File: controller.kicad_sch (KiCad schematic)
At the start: 50 parts, among them U1 TMC4671, U2 74LVC3G17, U3 74LVC3G17

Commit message: Small improvements.
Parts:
- added TP1: EN TestPoint, TestPoint:TestPoint_Pad_D1.0mm, symbol Connector:TestPoint
- C11, C12, C13, C14, C15, C16, C18, C19, C20, C21, C22, C35, C36, C40, C7, C8: MPN CL05B104KB54PNC -> GRM155R71H104KE14J
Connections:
- net DRV_EN: now also TP1.1
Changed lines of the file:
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@@
   (junction (at 149.86 162.56) (diameter 0) (color 0 0 0 0)
   )
+  (junction (at 180.34 26.67) (diameter 0) (color 0 0 0 0)
+  )
   (junction (at 54.61 104.14) (diameter 0) (color 0 0 0 0)
   )
@@
     (stroke (width 0) (type default))
   )
+  (wire (pts (xy 180.34 24.13) (xy 180.34 26.67))
+    (stroke (width 0) (type default))
+  )
   (wire (pts (xy 259.08 109.22) (xy 271.78 109.22))
     (stroke (width 0) (type default))
@@
     (stroke (width 0) (type default))
   )
+  (wire (pts (xy 180.34 26.67) (xy 177.8 26.67))
+    (stroke (width 0) (type default))
+  )
   (wire (pts (xy 234.95 128.27) (xy 232.41 128.27))
     (stroke (width 0) (type default))
@@
     (stroke (width 0) (type default))
   )
-  (wire (pts (xy 182.88 26.67) (xy 177.8 26.67))
+  (wire (pts (xy 182.88 26.67) (xy 180.34 26.67))
     (stroke (width 0) (type default))
   )
@@
       (effects (font (size 1.27 1.27)) hide)
     )
-    (property "MPN" "CL05B104KB54PNC" (at 107.95 167.64 0)
+    (property "MPN" "GRM155R71H104KE14J" (at 107.95 167.64 0)
       (effects (font (size 1.27 1.27)) hide)
     )
@@
       (effects (font (size 1.27 1.27)) hide)
     )
-    (property "MPN" "CL05B104KB54PNC" (at 54.61 128.27 0)
+    (property "MPN" "GRM155R71H104KE14J" (at 54.61 128.27 0)
       (effects (font (size 1.27 1.27)) hide)
     )
@@
       (effects (font (size 1.27 1.27)) hide)
     )
-    (property "MPN" "CL05B104KB54PNC" (at 218.44 162.56 0)
+    (property "MPN" "GRM155R71H104KE14J" (at 218.44 162.56 0)
       (effects (font (size 1.27 1.27)) hide)
     )
@@
       (effects (font (size 1.27 1.27)) hide)
     )
-    (property "MPN" "CL05B104KB54PNC" (at 93.98 167.64 0)
+    (property "MPN" "GRM155R71H104KE14J" (at 93.98 167.64 0)
       (effects (font (size 1.27 1.27)) hide)
     )
@@
       (effects (font (size 1.27 1.27)) hide)
     )
-    (property "MPN" "CL05B104KB54PNC" (at 135.89 167.64 0)
+    (property "MPN" "GRM155R71H104KE14J" (at 135.89 167.64 0)
       (effects (font (size 1.27 1.27)) hide)
     )
@@
       (effects (font (size 1.27 1.27)) hide)
     )
-    (property "MPN" "CL05B104KB54PNC" (at 33.02 157.48 0)
+    (property "MPN" "GRM155R71H104KE14J" (at 33.02 157.48 0)
       (effects (font (size 1.27 1.27)) hide)
     )
@@
       (effects (font (size 1.27 1.27)) hide)
     )
-    (property "MPN" "CL05B104KB54PNC" (at 73.66 86.36 0)
+    (property "MPN" "GRM155R71H104KE14J" (at 73.66 86.36 0)
       (effects (font (size 1.27 1.27)) hide)
     )
@@
       (effects (font (size 1.27 1.27)) hide)
     )
-    (property "MPN" "CL05B104KB54PNC" (at 121.92 167.64 0)
+    (property "MPN" "GRM155R71H104KE14J" (at 121.92 167.64 0)
       (effects (font (size 1.27 1.27)) hide)
     )
@@
       (effects (font (size 1.27 1.27)) hide)
     )
-    (property "MPN" "CL05B104KB54PNC" (at 39.37 128.27 0)
+    (property "MPN" "GRM155R71H104KE14J" (at 39.37 128.27 0)
       (effects (font (size 1.27 1.27)) hide)
     )
@@
       (effects (font (size 1.27 1.27)) hide)
     )
-    (property "MPN" "CL05B104KB54PNC" (at 69.85 109.22 0)
+    (property "MPN" "GRM155R71H104KE14J" (at 69.85 109.22 0)
       (effects (font (size 1.27 1.27)) hide)
     )
@@
       (effects (font (size 1.27 1.27)) hide)
     )
-    (property "MPN" "CL05B104KB54PNC" (at 149.86 167.64 0)
+    (property "MPN" "GRM155R71H104KE14J" (at 149.86 167.64 0)
       (effects (font (size 1.27 1.27)) hide)
     )
@@
       (effects (font (size 1.27 1.27)) hide)
     )
-    (property "MPN" "CL05B104KB54PNC" (at 217.17 38.1 0)
+    (property "MPN" "GRM155R71H104KE14J" (at 217.17 38.1 0)
       (effects (font (size 1.27 1.27)) hide)
     )
@@
     )
   )
+  (symbol (lib_id "Connector:TestPoint") (at 180.34 24.13 0) (unit 1)
+    (in_bom yes) (on_board yes) (dnp no) (fields_autoplaced)
+    (property "Reference" "TP1" (at 182.88 20.193 0)
+      (effects (font (size 1.27 1.27)) (justify left))
+    )
+    (property "Value" "EN TestPoint" (at 182.88 22.733 0)
+      (effects (font (size 1.27 1.27)) (justify left))
+    )
+    (property "Footprint" "TestPoint:TestPoint_Pad_D1.0mm" (at 185.42 24.13 0)
+      (effects (font (size 1.27 1.27)) hide)
+    )
+    (property "Datasheet" "~" (at 185.42 24.13 0)
+      (effects (font (size 1.27 1.27)) hide)
+    )
+    (pin "1")
+    (instances
+      (project "motor-driver"
+        (path "/314549f2-cc46-4559-991a-ae9411f3d209/25794513-4b05-4cf2-b97c-a9dcfa280e83"
+          (reference "TP1") (unit 1)
+        )
+      )
+    )
+  )
   (symbol (lib_id "74xGxx:74LVC3G17") (at 219.71 152.4 270) (unit 4)
     (in_bom yes) (on_board yes) (dnp no)
@@
       (effects (font (size 1.27 1.27)) hide)
     )
-    (property "MPN" "CL05B104KB54PNC" (at 31.75 40.64 0)
+    (property "MPN" "GRM155R71H104KE14J" (at 31.75 40.64 0)
       (effects (font (size 1.27 1.27)) hide)
     )
@@
       (effects (font (size 1.27 1.27)) hide)
     )
-    (property "MPN" "CL05B104KB54PNC" (at 69.85 128.27 0)
+    (property "MPN" "GRM155R71H104KE14J" (at 69.85 128.27 0)
       (effects (font (size 1.27 1.27)) hide)
     )
@@
       (effects (font (size 1.27 1.27)) hide)
     )
-    (property "MPN" "CL05B104KB54PNC" (at 33.02 186.69 0)
+    (property "MPN" "GRM155R71H104KE14J" (at 33.02 186.69 0)
       (effects (font (size 1.27 1.27)) hide)
     )
@@
       (effects (font (size 1.27 1.27)) hide)
     )
-    (property "MPN" "CL05B104KB54PNC" (at 163.83 167.64 0)
+    (property "MPN" "GRM155R71H104KE14J" (at 163.83 167.64 0)
       (effects (font (size 1.27 1.27)) hide)
     )

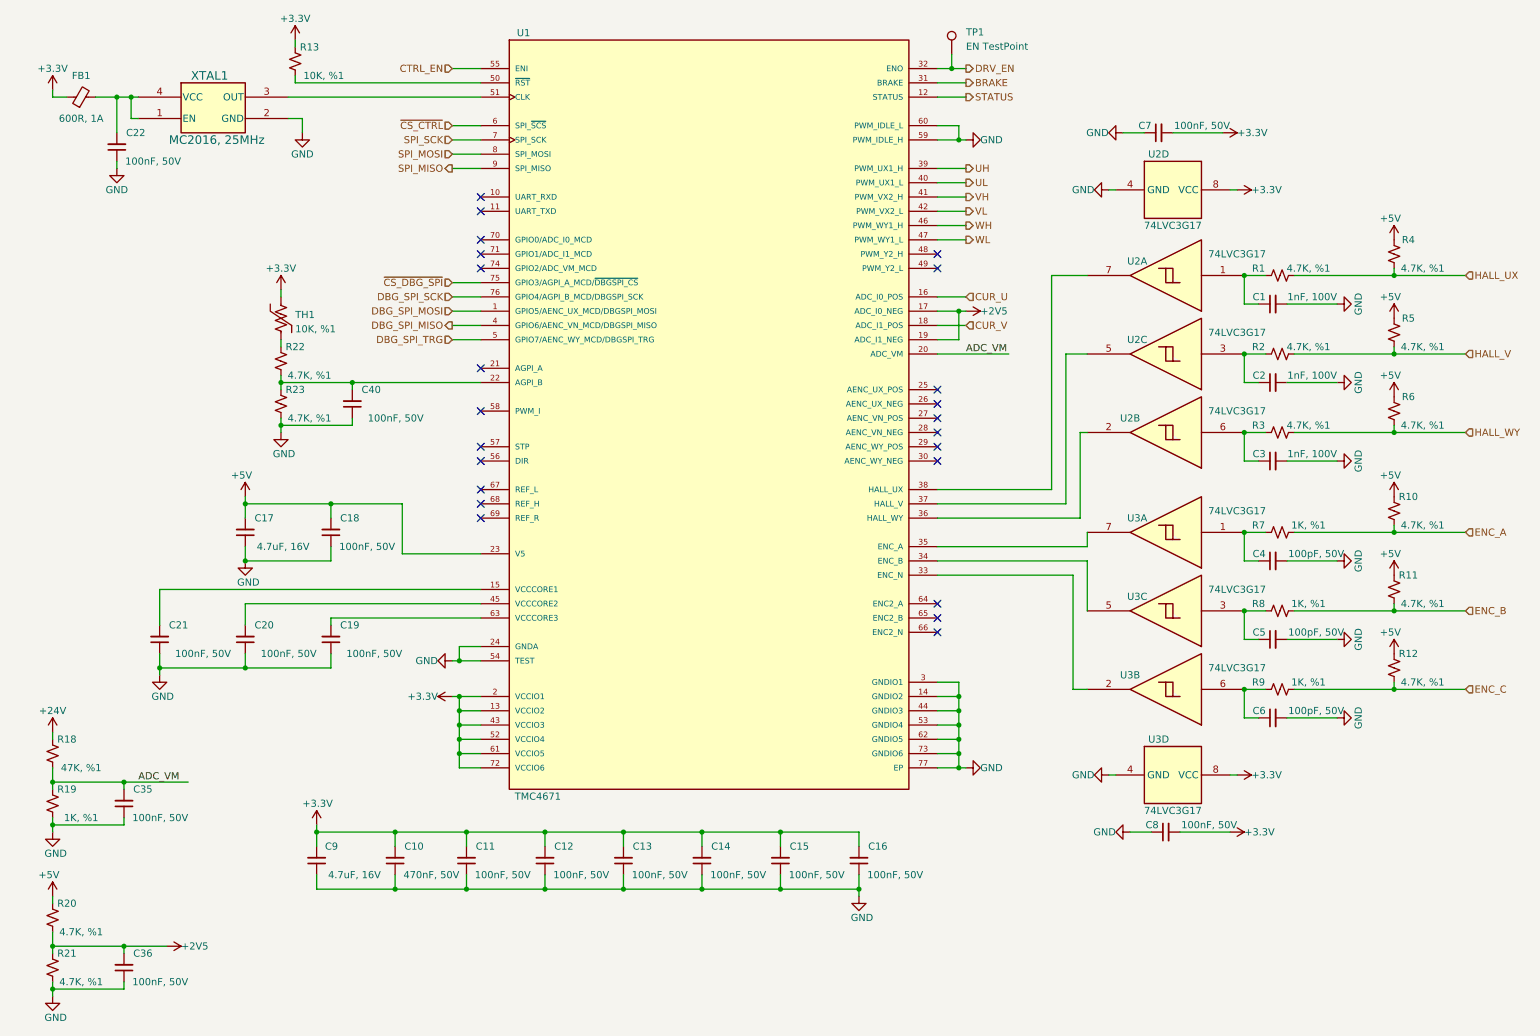
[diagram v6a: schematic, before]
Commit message: Optimize the BOM.
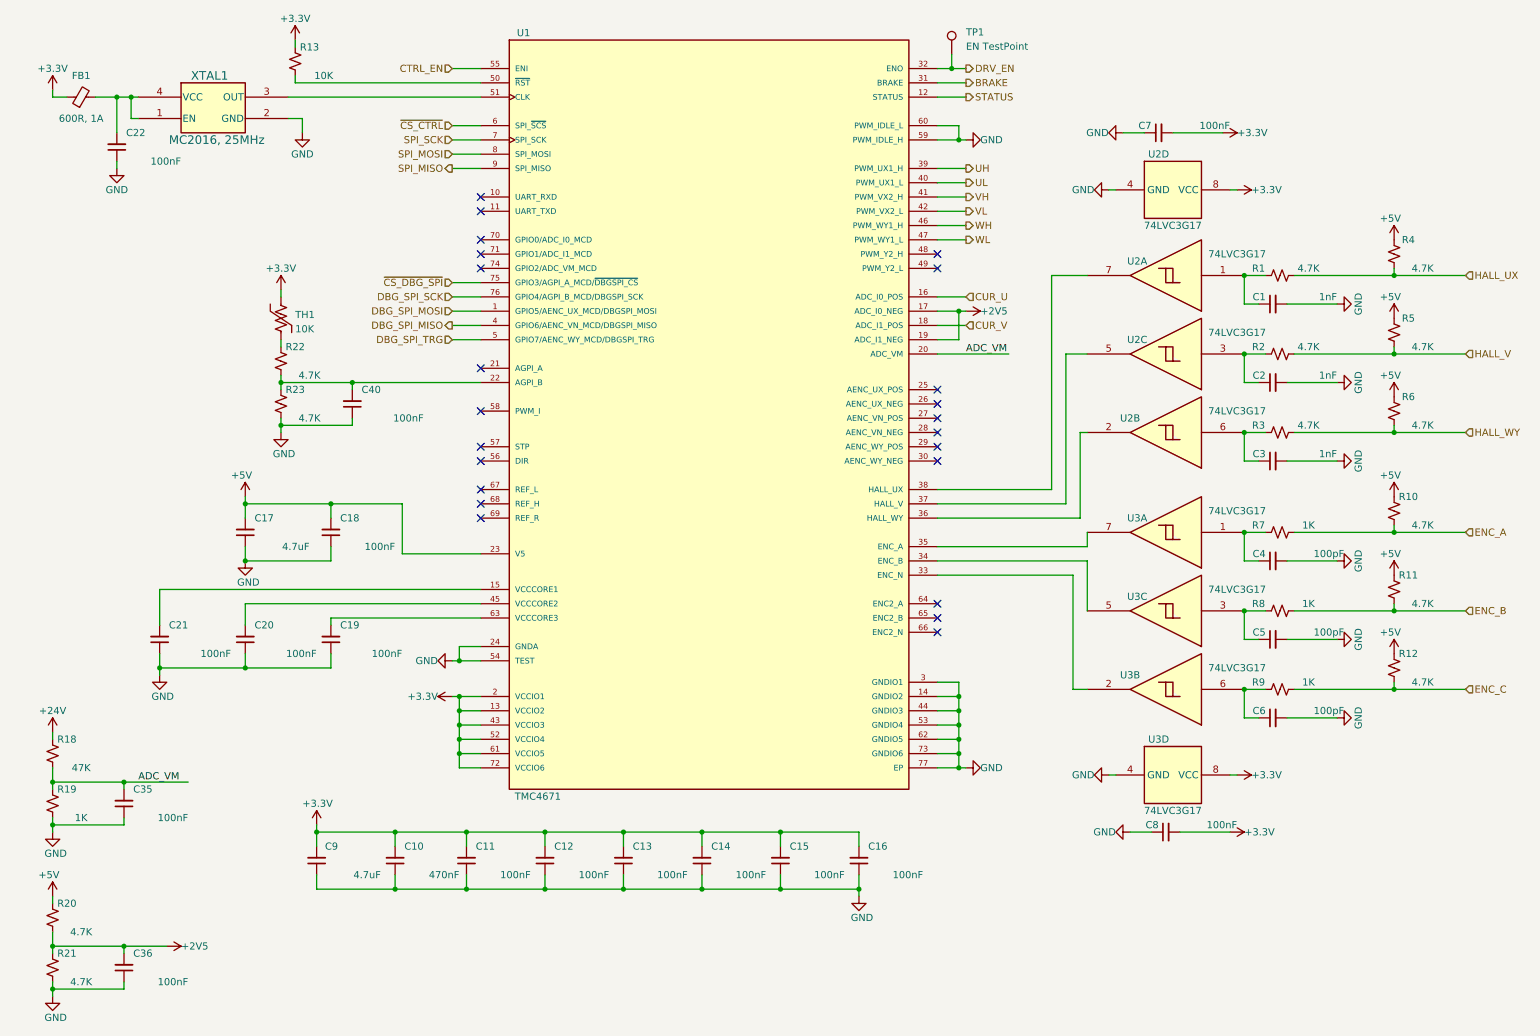
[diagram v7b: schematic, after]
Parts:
- C1, C2, C3: value 1nF, 100V -> 1nF
- C10: value 470nF, 50V -> 470nF; MPN C1608X7R1H474K080AC -> GRM188R71E474KA12J
- C11, C12, C13, C14, C15, C16, C18, C19, C20, C21, C22, C35, C36, C40, C7, C8: value 100nF, 50V -> 100nF
- C17, C9: value 4.7uF, 16V -> 4.7uF
- C4, C5, C6: value 100pF, 50V -> 100pF
- R1, R10, R11, R12, R2, R20, R21, R22, R23, R3, R4, R5, R6: value 4.7K, %1 -> 4.7K
- R13, TH1: value 10K, %1 -> 10K
- R18: value 47K, %1 -> 47K
- R19, R7, R8, R9: value 1K, %1 -> 1K
